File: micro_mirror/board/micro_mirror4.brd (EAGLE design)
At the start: 133.6 x 78.7 mm, 143 parts, among them IC1 74LV7014, IC2 74LV02, IC3 74LV08, IC5 LM324D, J1 POWER_JACKPTH_LOCK, U8 TPS62160, X1 SMA-142-0701-801/806, X2 SMA-142-0701-801/806, X3 SMA-142-0701-801/806, X4 SMA-142-0701-801/806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

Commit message: cleaning up schematic warnings
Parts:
- IC4: value (none) -> LMV324
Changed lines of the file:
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@@
 <attribute name="VALUE" x="36.195" y="67.31" size="1.27" layer="27"/>
 </element>
-<element name="IC4" library="micro_mirror3" package="LINEAR_SO14" value="" x="29.21" y="14.605" smashed="yes">
+<element name="IC4" library="micro_mirror3" package="LINEAR_SO14" value="LMV324" x="29.21" y="14.605" smashed="yes">
 <attribute name="NAME" x="28.575" y="15.113" size="1.27" layer="25" rot="R180"/>
 <attribute name="VALUE" x="35.052" y="12.7" size="1.27" layer="27" rot="R90"/>

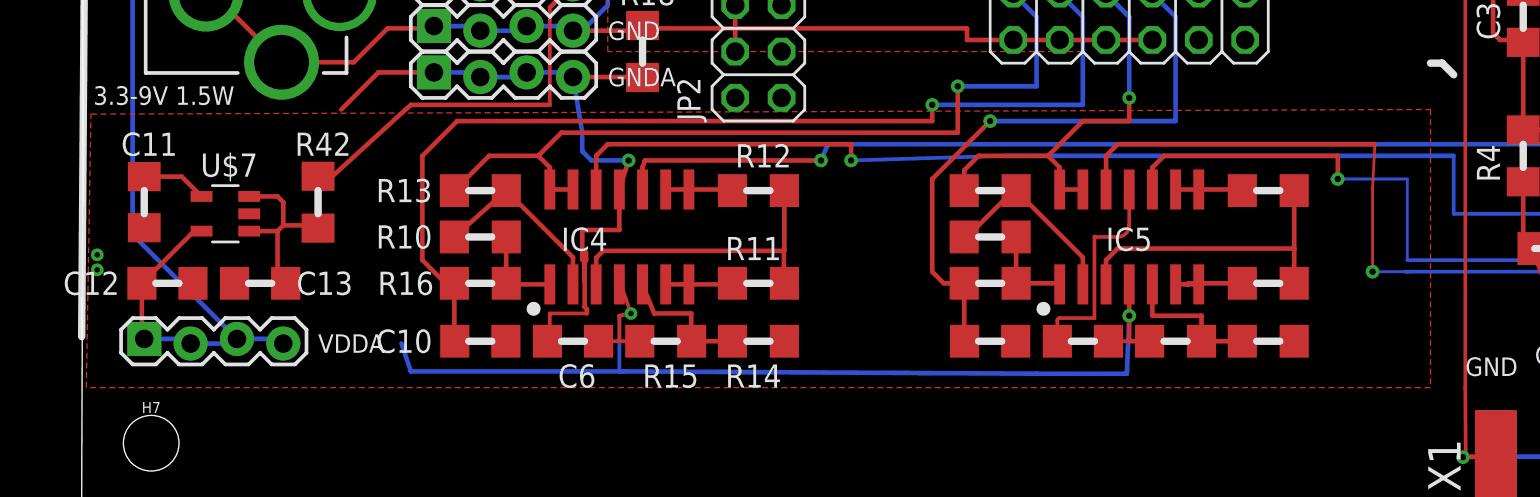
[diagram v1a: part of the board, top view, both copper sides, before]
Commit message: still need to do correct merge of vdd and vdda
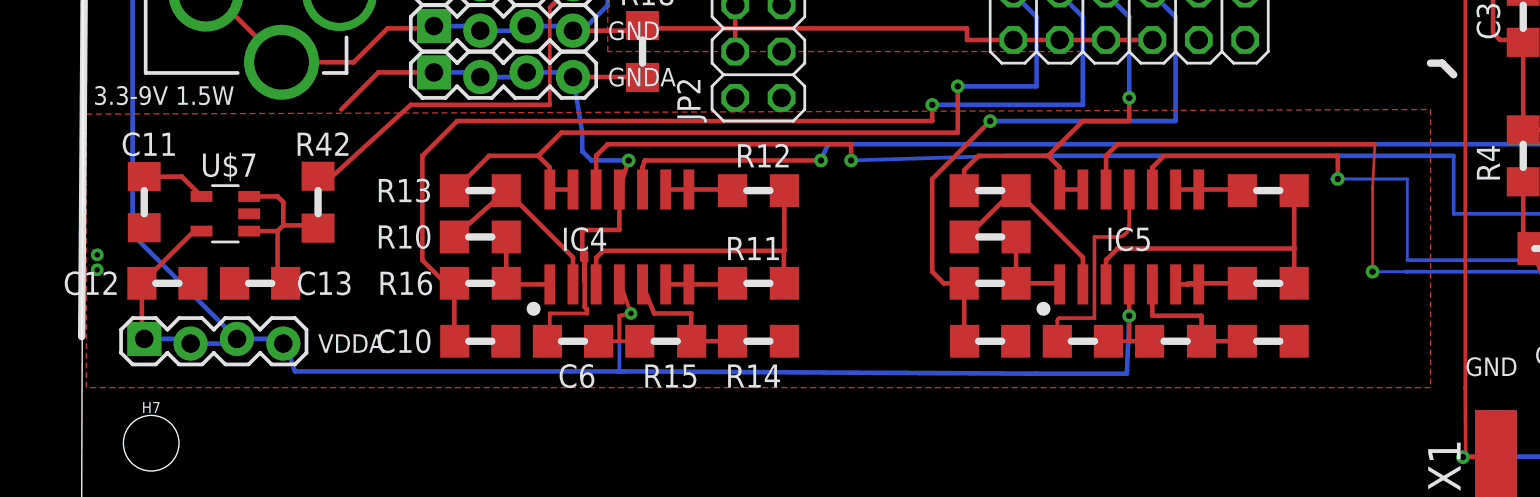
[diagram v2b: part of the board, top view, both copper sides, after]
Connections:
- net +3V3 renamed VDDA
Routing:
- net VDD: track 60.7 -> 67.1 mm
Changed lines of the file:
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@@
 <wire x1="35.348" y1="12.005" x2="35.408" y2="12.065" width="0.254" layer="1"/>
 </signal>
-<signal name="+3V3">
+<signal name="VDDA">
 <contactref element="C7" pad="1"/>
 <contactref element="IC1" pad="14"/>
@@
 <wire x1="56.134" y1="8.89" x2="56.01" y2="8.89" width="0.254" layer="1"/>
 <wire x1="57.15" y1="8.89" x2="58.268" y2="8.89" width="0.254" layer="1"/>
-<wire x1="17.272" y1="8.763" x2="17.78" y2="7.239" width="0.254" layer="16"/>
-<wire x1="17.78" y1="7.239" x2="29.21" y2="7.239" width="0.254" layer="16"/>
+<wire x1="10.922" y1="8.763" x2="11.43" y2="7.239" width="0.254" layer="16"/>
+<wire x1="11.43" y1="7.239" x2="29.21" y2="7.239" width="0.254" layer="16"/>
 <wire x1="29.21" y1="7.239" x2="29.464" y2="7.239" width="0.254" layer="16"/>
 <wire x1="29.464" y1="7.239" x2="52.07" y2="7.112" width="0.254" layer="16"/>
@@
 <contactref element="IC4" pad="11"/>
 <polygon width="0.254" layer="1" isolate="0.3048">
-<vertex x="0.254" y="21.336"/>
+<vertex x="0" y="21.336"/>
 <vertex x="73.66" y="21.59"/>
 <vertex x="73.66" y="6.35"/>

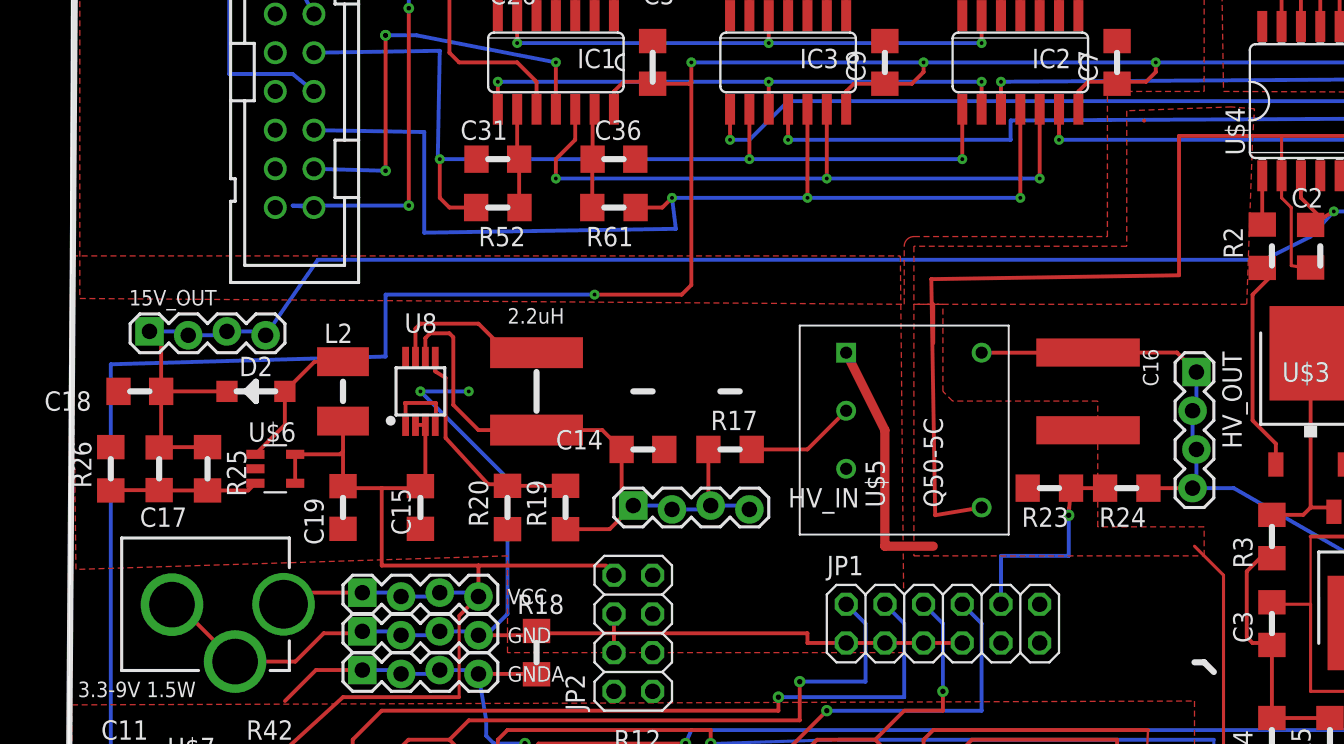
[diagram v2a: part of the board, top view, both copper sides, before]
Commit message: added voltage divider for HV out in case needed
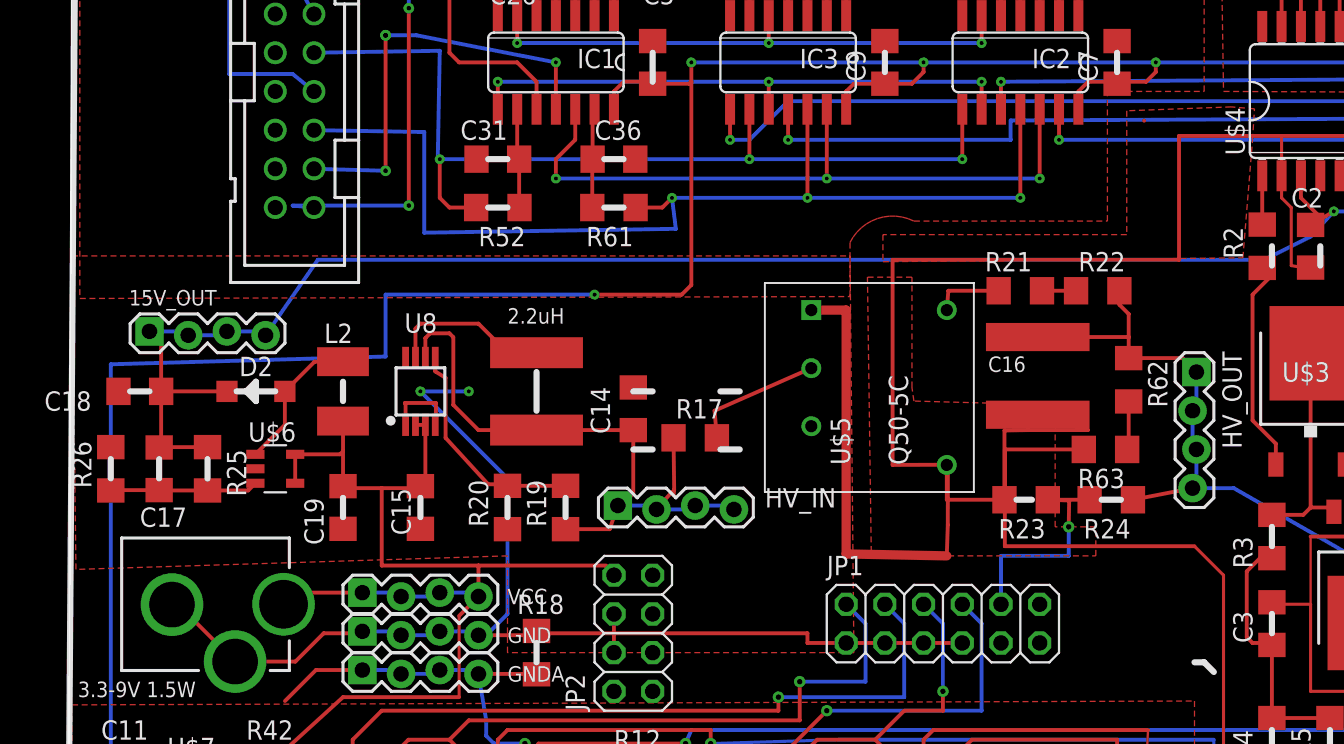
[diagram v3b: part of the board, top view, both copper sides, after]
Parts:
- added R21, R22: 510k, rcl:R1206
- added R62, R63: 10M, rcl:R1206
- moved U$5 3.61 mm to (48.5, 47.2)
- moved C16 3.45 mm to (63.4, 42.9)
- moved C14 2.74 mm to (36.8, 40.8), turned to 90 degrees
- moved R17 2.41 mm to (40.9, 38.9)
- moved R23 1.70 mm to (62.6, 34.8)
- moved R24 1.27 mm to (68.2, 34.8)
- moved HV_IN 1.02 mm to (35.8, 34.3)
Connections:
- new net N$24: R21.1, R22.1
- new net N$60: R21.2, U$5.3
- new net N$62: R62.2, R63.1
- net GND: now also R63.2
- net V+: now also R22.2, R62.1; no longer U$5.3
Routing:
- net GND: track 645.1 -> 700.6 mm
- net N$18: track 40.8 -> 48.1 mm
- net N$60: track 0.00 -> 4.58 mm
- net N$62: track 0.00 -> 3.19 mm
- net N$24: track 0.00 -> 2.24 mm
- net V+: track 91.6 -> 93.6 mm
- net N$12: track 7.25 -> 8.72 mm
- net HV_SENSE: track 14.3 -> 15.4 mm
